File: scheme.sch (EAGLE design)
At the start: 49 parts, among them J1 22-05-7048-04, J2 22-05-7028-02

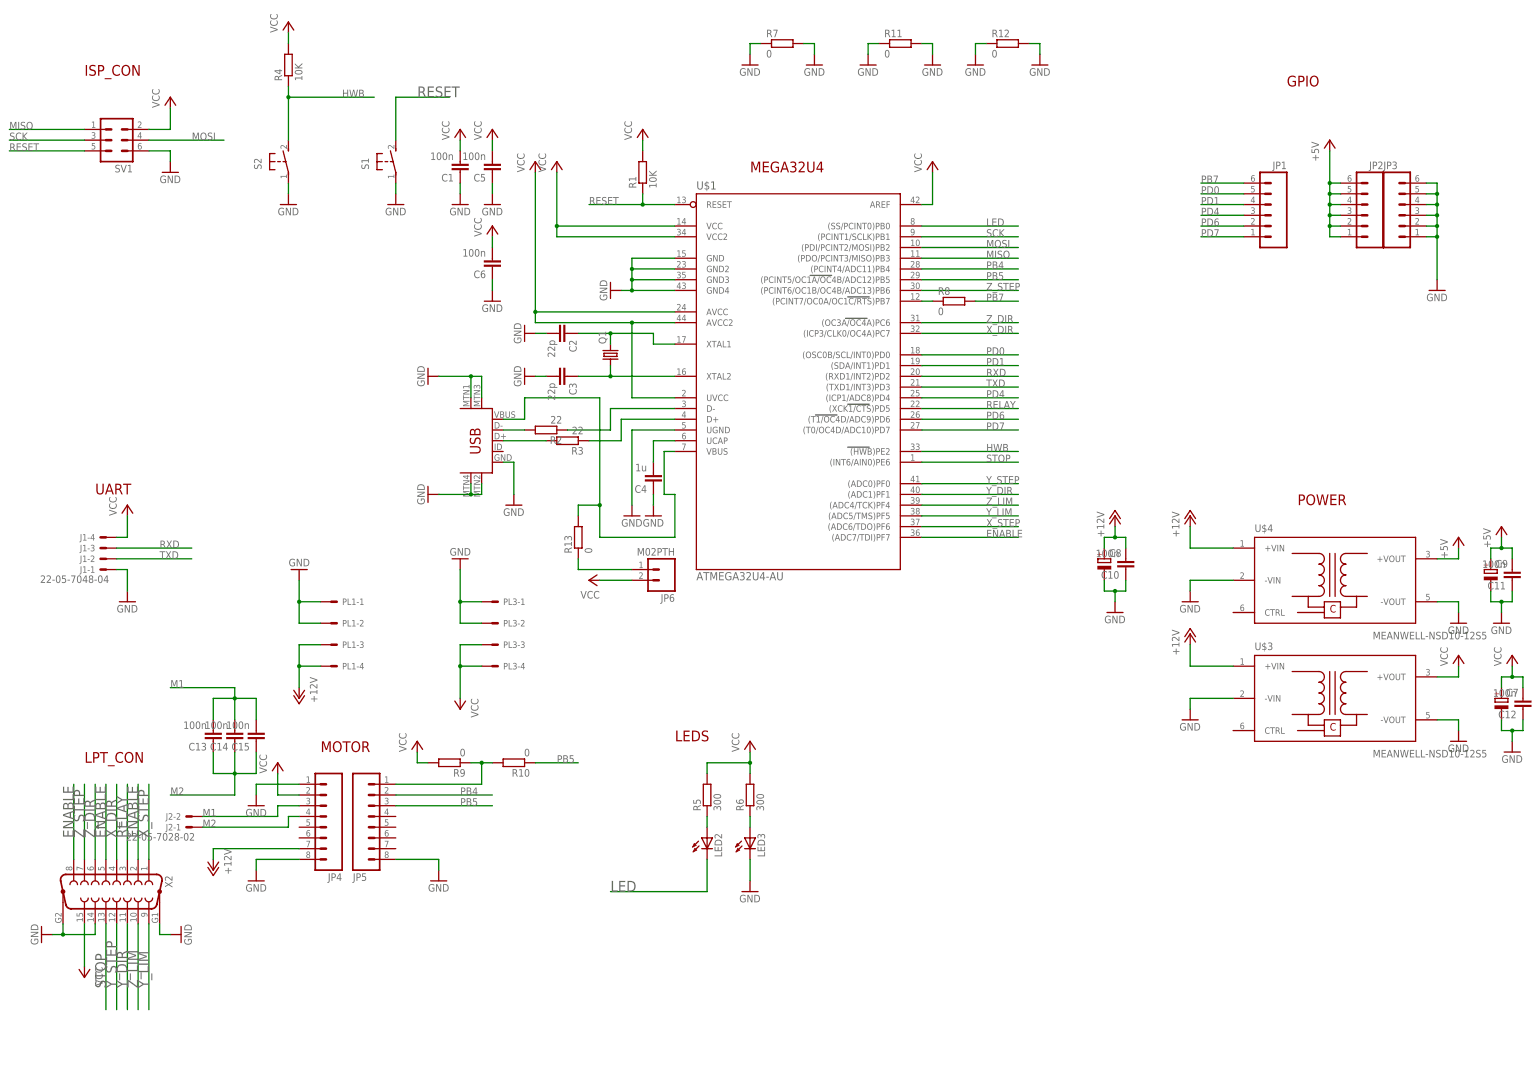
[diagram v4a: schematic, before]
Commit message: Fix DB-15 connector pinout for driver
Signed-off-by: Nikita 'webconn' Maslov <wkernelteam@gmail.com>
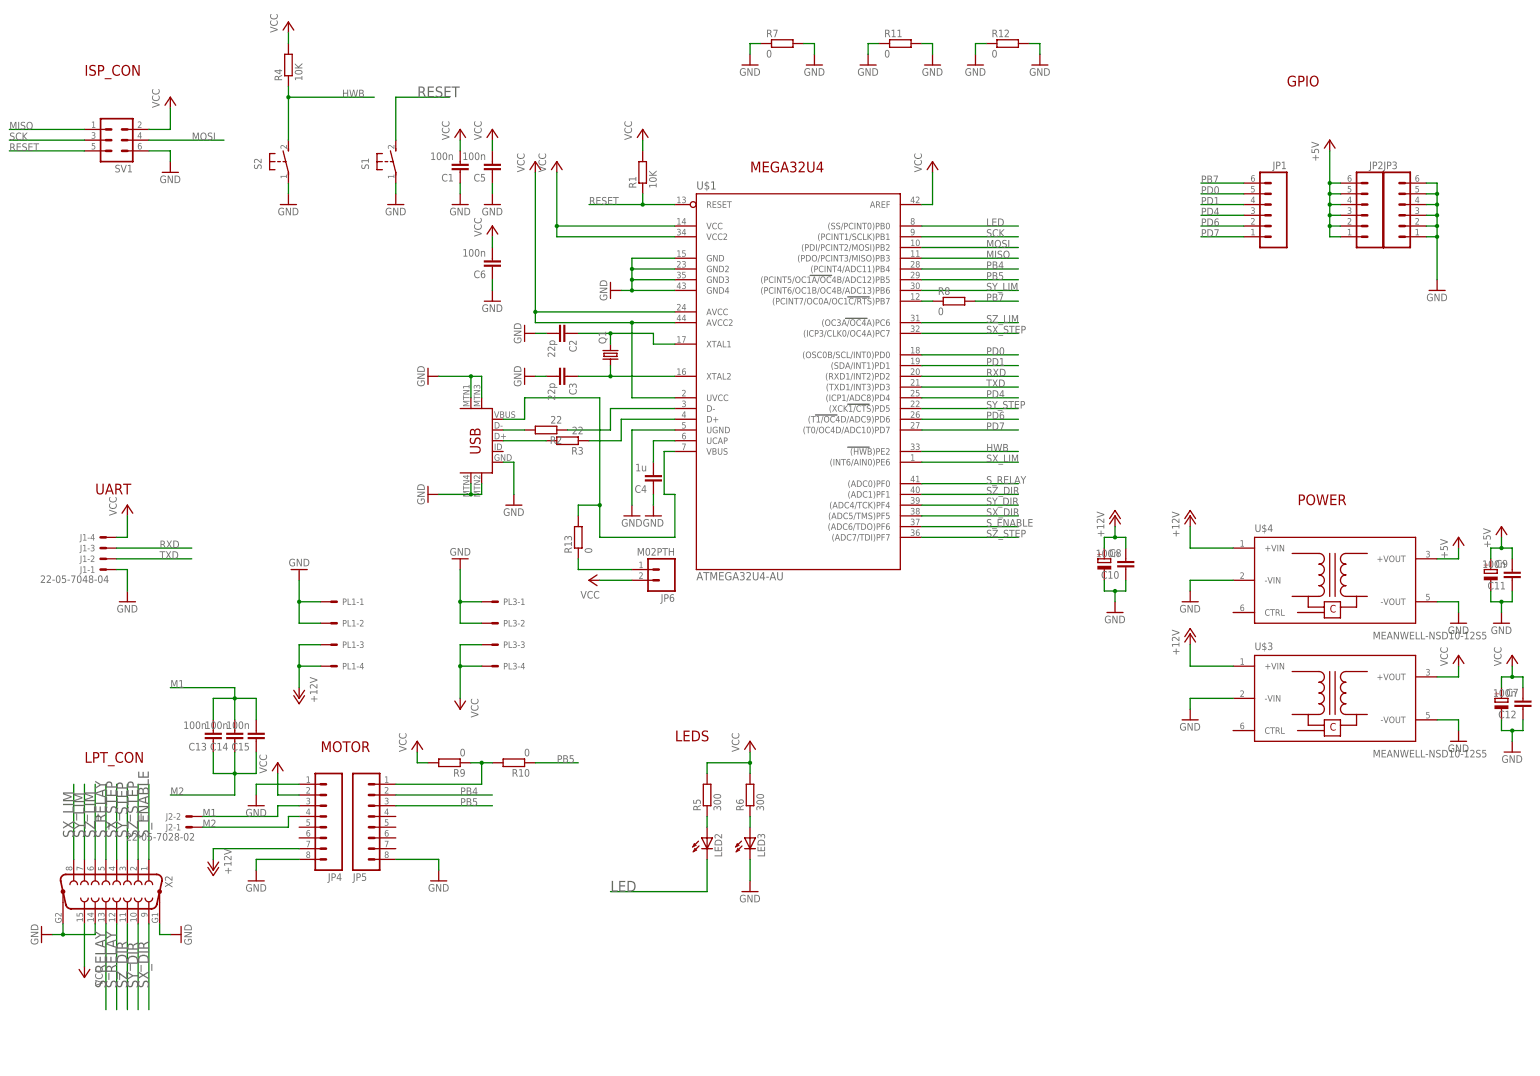
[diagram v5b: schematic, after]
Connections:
- net RELAY renamed SY_STEP
- net X_DIR renamed SX_STEP
- net X_STEP renamed S_ENABLE
- net Y_DIR renamed SZ_DIR
- net Y_LIM renamed SX_DIR
- net Z_DIR renamed SZ_LIM
- net Z_LIM renamed SY_DIR
- net Z_STEP renamed SY_LIM
- removed net ENABLE: U$1.(ADC7/TDI)PF7, X2.2, X2.5, X2.8
- removed net STOP: U$1.(INT6/AIN0)PE6, X2.13
- removed net Y_STEP: U$1.(ADC0)PF0, X2.12
- new net SX_LIM: U$1.(INT6/AIN0)PE6, X2.8
- new net SZ_STEP: U$1.(ADC7/TDI)PF7, X2.2
- new net S_RELAY: U$1.(ADC0)PF0, X2.12, X2.13, X2.5
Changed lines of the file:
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@@
 </segment>
 </net>
-<net name="ENABLE" class="0">
+<net name="SX_LIM" class="0">
 <segment>
 <pinref part="X2" gate="G$1" pin="8"/>
@@
 </segment>
 <segment>
-<pinref part="X2" gate="G$1" pin="5"/>
-<wire x1="43.18" y1="48.26" x2="43.18" y2="66.04" width="0.1524" layer="91"/>
-<label x="43.18" y="53.34" size="2.54" layer="95" rot="R90"/>
-</segment>
-<segment>
-<pinref part="X2" gate="G$1" pin="2"/>
-<wire x1="50.8" y1="48.26" x2="50.8" y2="66.04" width="0.1524" layer="91"/>
-<label x="50.8" y="53.34" size="2.54" layer="95" rot="R90"/>
-</segment>
-<segment>
-<pinref part="U$1" gate="G$1" pin="(ADC7/TDI)PF7"/>
-<wire x1="236.22" y1="124.46" x2="259.08" y2="124.46" width="0.1524" layer="91"/>
-<label x="251.46" y="124.46" size="1.778" layer="95"/>
-</segment>
-</net>
-<net name="Z_STEP" class="0">
+<pinref part="U$1" gate="G$1" pin="(INT6/AIN0)PE6"/>
+<wire x1="236.22" y1="142.24" x2="259.08" y2="142.24" width="0.1524" layer="91"/>
+<label x="251.46" y="142.24" size="1.778" layer="95"/>
+</segment>
+</net>
+<net name="SY_LIM" class="0">
 <segment>
 <pinref part="X2" gate="G$1" pin="7"/>
@@
 </segment>
 </net>
-<net name="Z_DIR" class="0">
+<net name="SZ_LIM" class="0">
 <segment>
 <pinref part="X2" gate="G$1" pin="6"/>
@@
 </segment>
 </net>
-<net name="X_DIR" class="0">
+<net name="SX_STEP" class="0">
 <segment>
 <pinref part="X2" gate="G$1" pin="4"/>
@@
 </segment>
 </net>
-<net name="RELAY" class="0">
+<net name="SY_STEP" class="0">
 <segment>
 <pinref part="X2" gate="G$1" pin="3"/>
@@
 </segment>
 </net>
-<net name="X_STEP" class="0">
+<net name="S_ENABLE" class="0">
 <segment>
 <pinref part="X2" gate="G$1" pin="1"/>
@@
 </segment>
 </net>
-<net name="Y_LIM" class="0">
+<net name="SX_DIR" class="0">
 <segment>
 <pinref part="X2" gate="G$1" pin="9"/>
@@
 </segment>
 </net>
-<net name="Z_LIM" class="0">
+<net name="SY_DIR" class="0">
 <segment>
 <pinref part="X2" gate="G$1" pin="10"/>
@@
 </segment>
 </net>
-<net name="Y_DIR" class="0">
+<net name="SZ_DIR" class="0">
 <segment>
 <pinref part="X2" gate="G$1" pin="11"/>
@@
 <wire x1="236.22" y1="134.62" x2="259.08" y2="134.62" width="0.1524" layer="91"/>
 <label x="251.46" y="134.62" size="1.778" layer="95"/>
-</segment>
-</net>
-<net name="Y_STEP" class="0">
-<segment>
-<pinref part="X2" gate="G$1" pin="12"/>
-<wire x1="45.72" y1="33.02" x2="45.72" y2="12.7" width="0.1524" layer="91"/>
-<label x="45.72" y="17.78" size="2.54" layer="95" rot="R90"/>
-</segment>
-<segment>
-<pinref part="U$1" gate="G$1" pin="(ADC0)PF0"/>
-<wire x1="236.22" y1="137.16" x2="259.08" y2="137.16" width="0.1524" layer="91"/>
-<label x="251.46" y="137.16" size="1.778" layer="95"/>
-</segment>
-</net>
-<net name="STOP" class="0">
-<segment>
-<pinref part="X2" gate="G$1" pin="13"/>
-<wire x1="43.18" y1="33.02" x2="43.18" y2="12.7" width="0.1524" layer="91"/>
-<label x="43.18" y="17.78" size="2.54" layer="95" rot="R90"/>
-</segment>
-<segment>
-<pinref part="U$1" gate="G$1" pin="(INT6/AIN0)PE6"/>
-<wire x1="236.22" y1="142.24" x2="259.08" y2="142.24" width="0.1524" layer="91"/>
-<label x="251.46" y="142.24" size="1.778" layer="95"/>
 </segment>
 </net>
@@
 </segment>
 </net>
+<net name="SZ_STEP" class="0">
+<segment>
+<pinref part="X2" gate="G$1" pin="2"/>
+<wire x1="50.8" y1="48.26" x2="50.8" y2="66.04" width="0.1524" layer="91"/>
+<label x="50.8" y="53.34" size="2.54" layer="95" rot="R90"/>
+</segment>
+<segment>
+<pinref part="U$1" gate="G$1" pin="(ADC7/TDI)PF7"/>
+<wire x1="236.22" y1="124.46" x2="259.08" y2="124.46" width="0.1524" layer="91"/>
+<label x="251.46" y="124.46" size="1.778" layer="95"/>
+</segment>
+</net>
+<net name="S_RELAY" class="0">
+<segment>
+<pinref part="X2" gate="G$1" pin="5"/>
+<wire x1="43.18" y1="48.26" x2="43.18" y2="66.04" width="0.1524" layer="91"/>
+<label x="43.18" y="53.34" size="2.54" layer="95" rot="R90"/>
+</segment>
+<segment>
+<pinref part="U$1" gate="G$1" pin="(ADC0)PF0"/>
+<wire x1="236.22" y1="137.16" x2="259.08" y2="137.16" width="0.1524" layer="91"/>
+<label x="251.46" y="137.16" size="1.778" layer="95"/>
+</segment>
+<segment>
+<pinref part="X2" gate="G$1" pin="13"/>
+<wire x1="43.18" y1="33.02" x2="43.18" y2="12.7" width="0.1524" layer="91"/>
+<label x="43.18" y="17.78" size="2.54" layer="95" rot="R90"/>
+</segment>
+<segment>
+<pinref part="X2" gate="G$1" pin="12"/>
+<wire x1="45.72" y1="33.02" x2="45.72" y2="12.7" width="0.1524" layer="91"/>
+<label x="45.72" y="17.78" size="2.54" layer="95" rot="R90"/>
+</segment>
+</net>
